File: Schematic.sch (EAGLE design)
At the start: 61 parts, among them IC1 TL082, IC2 PIC18F2550_28DIP, IC3 7812, IC4 7805, IC5 7912, IC6 TL082, K1 G5L, Q1 20 mhz, T1 BC548, X2 FUENTE

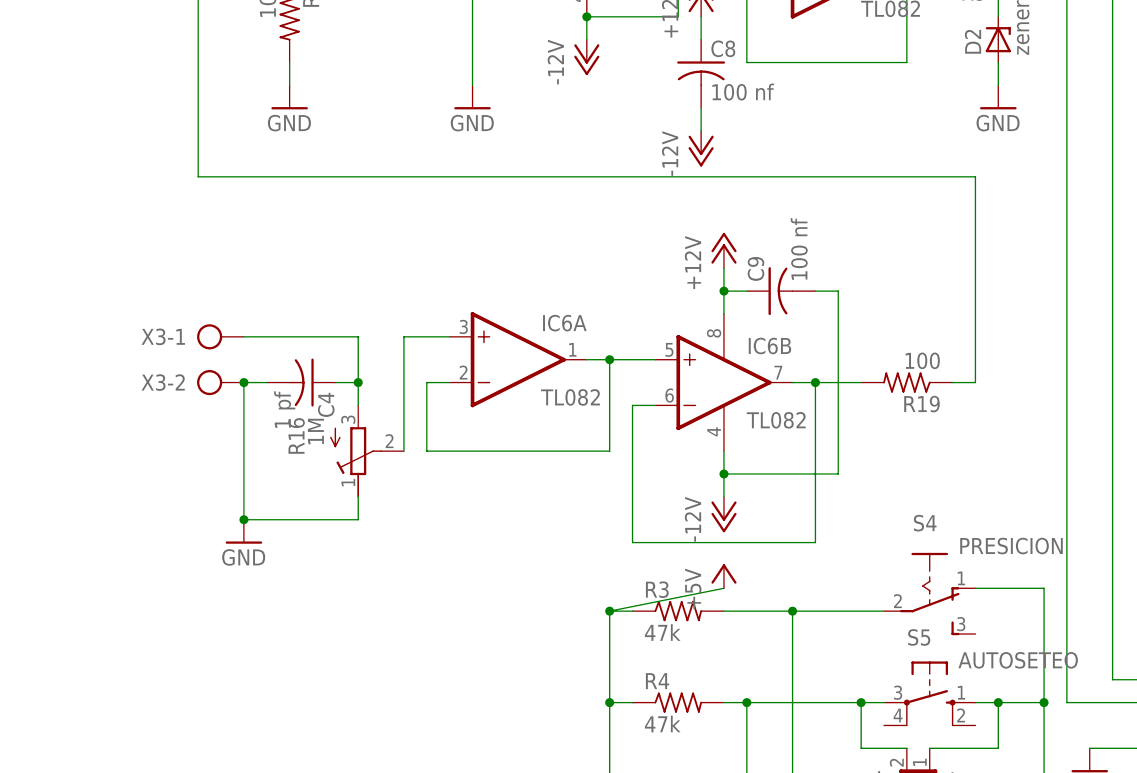
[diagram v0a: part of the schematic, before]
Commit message: Ver 2
Algorithm: I applied some filters.
Board and scheme: I implemented a balanced opamp circuit that proof to by less noisy.
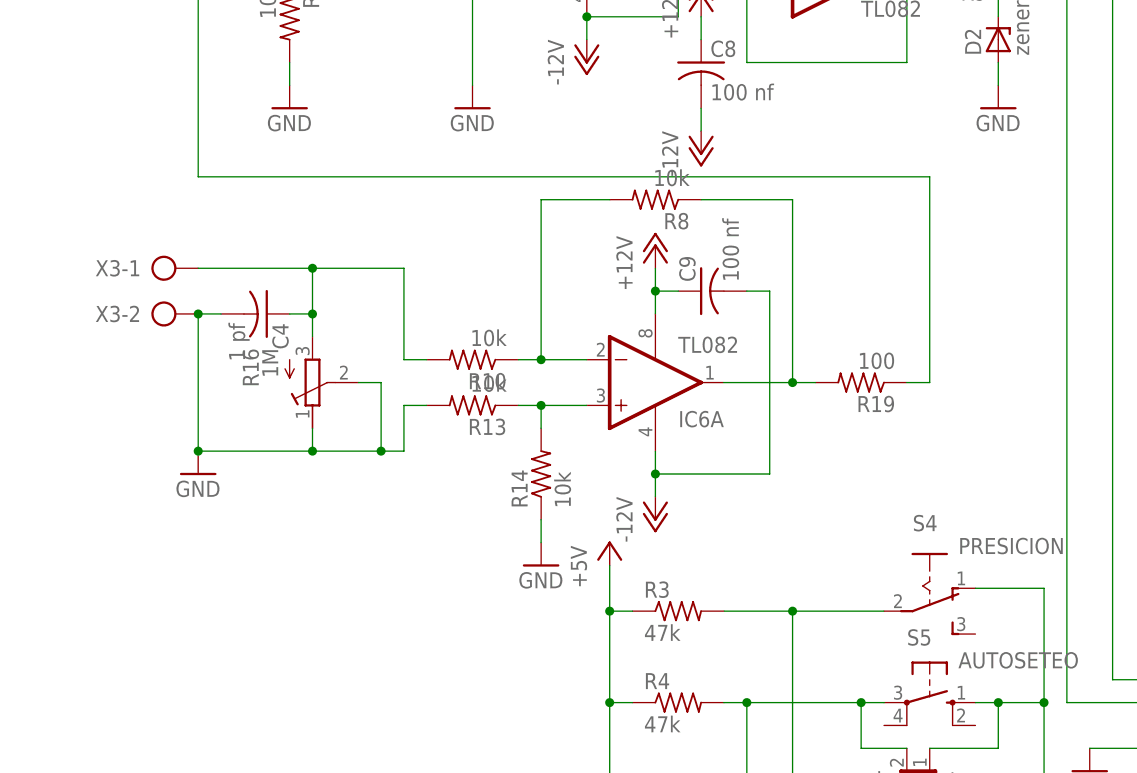
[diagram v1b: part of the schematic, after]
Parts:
- added R10, R13, R14, R8: 10k, resistor:R-US_0207/10
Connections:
- net GND: now also R13.2, R14.1, R16.S
- net N$1: now also IC6A.+IN, R13.1, R14.2; no longer IC6A.-IN, IC6A.OUT, IC6B.+IN
- net N$21: now also IC6A.OUT, R8.1; no longer IC6B.-IN, IC6B.OUT
- net N$51: now also R10.2
- net N$7: now also IC6A.-IN, R10.1, R8.2; no longer IC6A.+IN, R16.S
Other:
- moved on the sheet: C4, C9, IC6A, R16, R19, X3-1, X3-2
